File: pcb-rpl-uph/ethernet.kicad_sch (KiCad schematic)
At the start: 0 parts

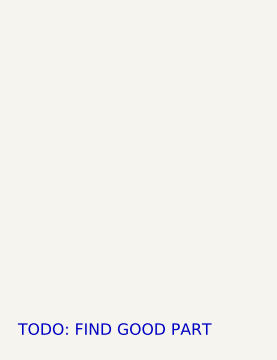
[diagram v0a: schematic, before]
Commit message: Add ethernet
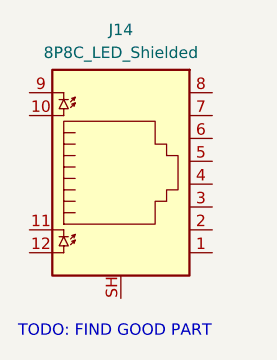
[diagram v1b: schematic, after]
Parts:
- added J14: 8P8C_LED_Shielded, Connector_RJ:RJ45_Amphenol_RJHSE538X, symbol Connector:8P8C_LED_Shielded
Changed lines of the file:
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@@
     (effects (font (size 1.27 1.27)) (justify left bottom))
   )
+  (symbol (lib_id "Connector:8P8C_LED_Shielded") (at 142.875 76.835 0) (unit 1)
+    (in_bom yes) (on_board yes) (dnp no) (fields_autoplaced)
+    (property "Reference" "J14" (at 142.875 59.69 0)
+      (effects (font (size 1.27 1.27)))
+    )
+    (property "Value" "8P8C_LED_Shielded" (at 142.875 62.23 0)
+      (effects (font (size 1.27 1.27)))
+    )
+    (property "Footprint" "Connector_RJ:RJ45_Amphenol_RJHSE538X" (at 142.875 76.2 90)
+      (effects (font (size 1.27 1.27)) hide)
+    )
+    (property "Datasheet" "~" (at 142.875 76.2 90)
+      (effects (font (size 1.27 1.27)) hide)
+    )
+    (pin "1")
+    (pin "10")
+    (pin "11")
+    (pin "12")
+    (pin "2")
+    (pin "3")
+    (pin "4")
+    (pin "5")
+    (pin "6")
+    (pin "7")
+    (pin "8")
+    (pin "9")
+    (pin "SH")
+    (instances
+      (project "virgo-rpl-uph"
+        (path "/16b1e6ca-a3e2-42a7-b57e-a744c26a548a/4dfda455-f6e0-47b2-93c0-a5a0b481609e"
+          (reference "J14") (unit 1)
+        )
+      )
+    )
+  )
 )
